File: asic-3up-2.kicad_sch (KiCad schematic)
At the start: 64 parts, among them J16 Conn_01x01, J17 Conn_01x01, J8 Conn_01x01, J9 Conn_01x01, U57 MCP1824T-1202E/OT, U58 MCP1824T-1202E/OT, U59 MCP1824T-1202E/OT, U60 MCP1824T-0802E, U61 MCP1824T-0802E, U62 MCP1824T-0802E, U63 BM1362AC_MODE1, U64 BM1362AC_MODE0, U65 BM1362AC_MODE1

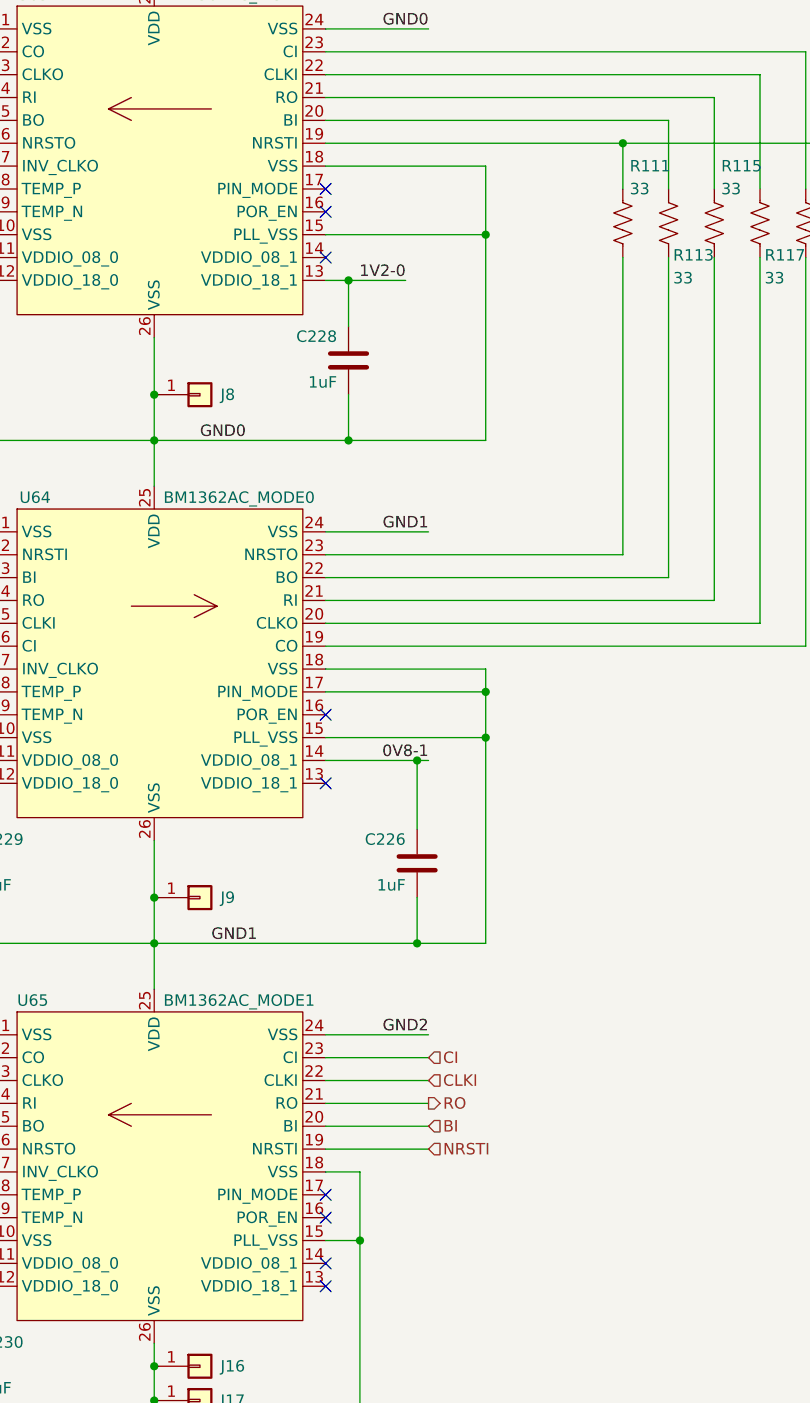
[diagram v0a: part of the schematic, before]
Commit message: fix PIN_MODE connections for #17
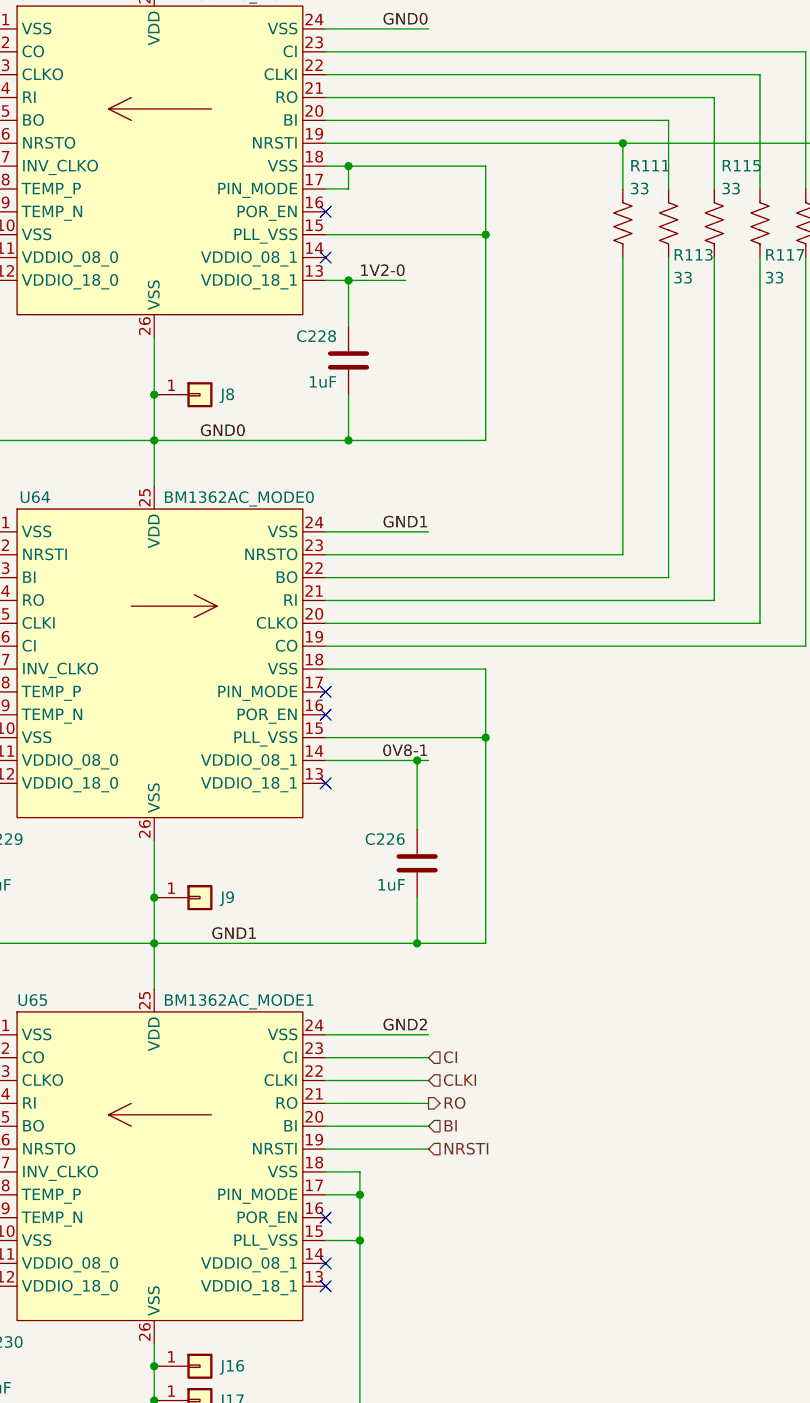
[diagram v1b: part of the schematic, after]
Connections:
- net GND0: now also U63.17 (PIN_MODE)
- net GND1: no longer U64.17 (PIN_MODE)
- net VSS: now also U65.17 (PIN_MODE)
- no-connect marks 26 -> 25
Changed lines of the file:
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@@
+	)
+	(junction
+		(at 271.78 186.69)
+		(diameter 0)
+		(color 0 0 0 0)
 	)
 	(junction
@@
 	)
 	(junction
-		(at 285.75 130.81)
-		(diameter 0)
-		(color 0 0 0 0)
-	)
-	(junction
 		(at 248.92 153.67)
 		(diameter 0)
@@
 	)
 	(junction
+		(at 270.51 72.39)
+		(diameter 0)
+		(color 0 0 0 0)
+	)
+	(junction
 		(at 87.63 137.16)
 		(diameter 0.9144)
@@
 	)
 	(no_connect
-		(at 267.97 186.69)
-	)
-	(no_connect
 		(at 267.97 82.55)
 	)
@@
 	)
 	(no_connect
+		(at 267.97 130.81)
+	)
+	(no_connect
 		(at 231.14 138.43)
 	)
@@
 	)
 	(no_connect
-		(at 267.97 74.93)
-	)
-	(no_connect
 		(at 66.04 185.42)
 	)
@@
 	(wire
 		(pts
-			(xy 285.75 72.39) (xy 267.97 72.39)
+			(xy 285.75 72.39) (xy 270.51 72.39)
+		)
+		(stroke
+			(width 0)
+			(type default)
+		)
+	)
+	(wire
+		(pts
+			(xy 270.51 72.39) (xy 267.97 72.39)
 		)
 		(stroke
@@
 	(wire
 		(pts
-			(xy 285.75 130.81) (xy 285.75 128.27)
+			(xy 267.97 186.69) (xy 271.78 186.69)
 		)
 		(stroke
@@
 	(wire
 		(pts
+			(xy 270.51 74.93) (xy 270.51 72.39)
+		)
+		(stroke
+			(width 0)
+			(type default)
+		)
+	)
+	(wire
+		(pts
 			(xy 219.71 82.55) (xy 220.98 82.55)
 		)
@@
 	(wire
 		(pts
+			(xy 267.97 74.93) (xy 270.51 74.93)
+		)
+		(stroke
+			(width 0)
+			(type default)
+		)
+	)
+	(wire
+		(pts
 			(xy 152.4 74.93) (xy 152.4 78.74)
 		)
@@
 	(wire
 		(pts
-			(xy 285.75 135.89) (xy 285.75 130.81)
+			(xy 285.75 128.27) (xy 285.75 135.89)
 		)
 		(stroke
@@
 	(wire
 		(pts
-			(xy 267.97 130.81) (xy 285.75 130.81)
-		)
-		(stroke
-			(width 0)
-			(type default)
-		)
-	)
-	(wire
-		(pts
 			(xy 270.51 85.09) (xy 267.97 85.09)
 		)
@@
 	(wire
 		(pts
+			(xy 271.78 186.69) (xy 271.78 191.77)
+		)
+		(stroke
+			(width 0)
+			(type default)
+		)
+	)
+	(wire
+		(pts
 			(xy 205.74 123.19) (xy 205.74 130.81)
 		)
@@
 	(wire
 		(pts
-			(xy 271.78 184.15) (xy 271.78 191.77)
-		)
-		(stroke
+			(xy 271.78 184.15) (xy 271.78 186.69)
+		)
+		(stroke

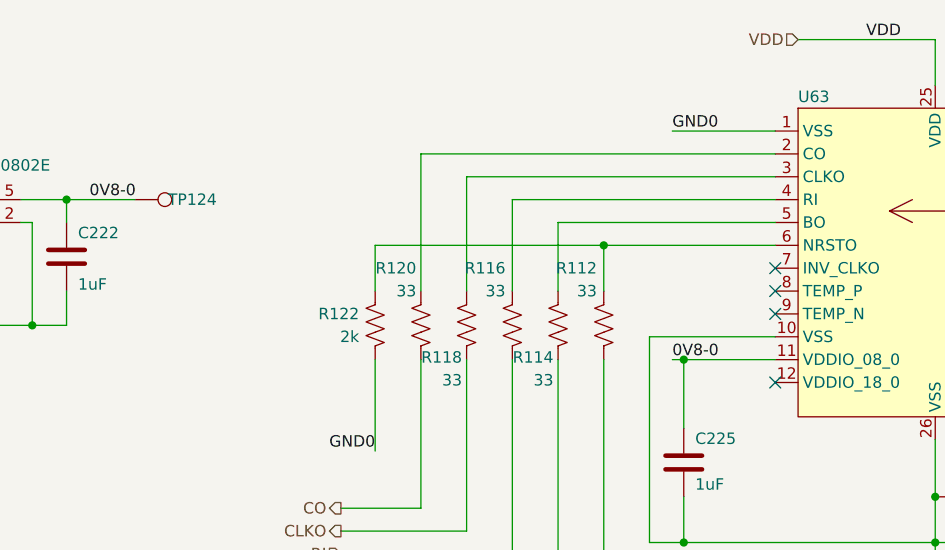
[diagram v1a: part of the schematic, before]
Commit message: added RI pullup resistors for #16. updated BOM. bumped version number to 3
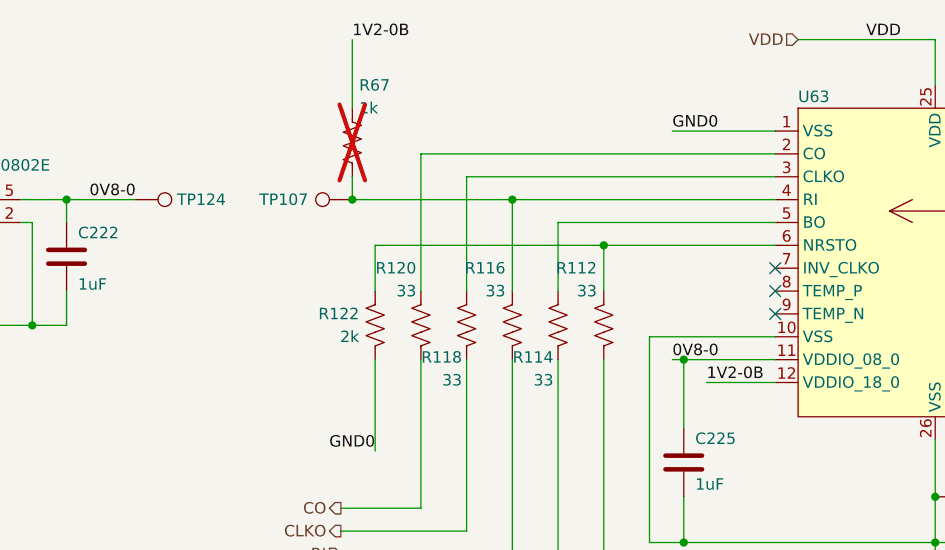
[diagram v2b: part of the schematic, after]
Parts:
- added R67: 1k, Resistor_SMD:R_0402_1005Metric, symbol Device:R_US
- added TP107: TestPoint, TestPoint:TestPoint_Pad_D1.0mm, symbol Connector:TestPoint
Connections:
- net 1V2-0B: now reaches U63.12 (VDDIO_18_0)
- net 1V2-0B: now also R67.1
- net at R116.1, U63.4 (RI): now also R67.2, TP107.1
- no-connect marks 25 -> 24
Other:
- title: (none) -> emberOne/00
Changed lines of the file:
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@@
 	(paper "A3")
 	(title_block
-		(date "2024-11-25")
-		(rev "2")
+		(title "emberOne/00")
+		(date "2025-02-25")
+		(rev "3")
 	)
 	(text "Reference Voltage Regulators"
@@
 	)
 	(junction
+		(at 201.93 64.77)
+		(diameter 0)
+		(color 0 0 0 0)
+	)
+	(junction
 		(at 356.87 114.3)
 		(diameter 0)
@@
 	)
 	(junction
+		(at 184.15 64.77)
+		(diameter 0)
+		(color 0 0 0 0)
+	)
+	(junction
 		(at 285.75 80.01)
 		(diameter 0)
@@
 	)
 	(no_connect
-		(at 231.14 85.09)
-	)
-	(no_connect
 		(at 231.14 184.15)
 	)
@@
 	(wire
 		(pts
+			(xy 184.15 46.99) (xy 184.15 54.61)
+		)
+		(stroke
+			(width 0)
+			(type default)
+		)
+	)
+	(wire
+		(pts
 			(xy 267.97 125.73) (xy 321.31 125.73)
 		)
@@
 	(wire
 		(pts
+			(xy 184.15 64.77) (xy 184.15 62.23)
+		)
+		(stroke
+			(width 0)
+			(type default)
+		)
+	)
+	(wire
+		(pts
 			(xy 270.51 85.09) (xy 267.97 85.09)
 		)
@@
 	(wire
 		(pts
+			(xy 184.15 64.77) (xy 201.93 64.77)
+		)
+		(stroke
+			(width 0)
+			(type default)
+		)
+	)
+	(wire
+		(pts
 			(xy 91.44 133.35) (xy 91.44 137.16)
 		)
@@
 	(wire
 		(pts
+			(xy 223.52 85.09) (xy 231.14 85.09)
+		)
+		(stroke
+			(width 0)
+			(type default)
+		)
+	)
+	(wire
+		(pts
 			(xy 248.92 153.67) (xy 248.92 158.75)
 		)
@@
 		)
 	)
+	(label "1V2-0B"
+		(at 184.15 46.99 0)
+		(effects
+			(font
+				(size 1.27 1.27)
+			)
+			(justify left bottom)
+		)
+	)
+	(label "1V2-0B"
+		(at 223.52 85.09 0)
+		(effects
+			(font
+				(size 1.27 1.27)
+			)
+			(justify left bottom)
+		)
+	)
 	(label "1V2-0"
 		(at 276.86 85.09 180)
@@
 	)
 	(symbol
+		(lib_id "Connector:TestPoint")
+		(at 184.15 64.77 90)
+		(mirror x)
+		(unit 1)
+		(exclude_from_sim no)
+		(in_bom no)
+		(on_board yes)
+		(dnp no)
+		(property "Reference" "TP107"
+			(at 176.53 64.77 90)
+			(effects
+				(font
+					(size 1.27 1.27)
+				)
+			)
+		)
+		(property "Value" "TestPoint"
+			(at 178.435 66.0399 90)
+			(effects
+				(font
+					(size 1.27 1.27)
+				)
+				(justify left)
+				(hide yes)
+			)
+		)
+		(property "Footprint" "TestPoint:TestPoint_Pad_D1.0mm"
+			(at 184.15 69.85 0)
+			(effects
+				(font
+					(size 1.27 1.27)
+				)
+				(hide yes)
+			)
+		)
+		(property "Datasheet" "~"
+			(at 184.15 69.85 0)
+			(effects
+				(font
+					(size 1.27 1.27)
+				)
+				(hide yes)
+			)
+		)
+		(property "Description" ""
+			(at 184.15 64.77 0)
+			(effects
+				(font
+					(size 1.27 1.27)
+				)
+				(hide yes)
+			)
+		)
+		(pin "1"
+		)
+		(instances
+			(project "emberone"
+				(path "/b036224c-4cdf-48cc-81df-19bc5283ebd2/b7ad7cc6-371f-46f9-875b-8b04bdc75b20"
+					(reference "TP107")
+					(unit 1)
+				)
+			)
+		)
+	)
+	(symbol
 		(lib_id "Device:C")
 		(at 346.71 72.39 0)
@@
 	)
 	(symbol
+		(lib_id "Device:R_US")
+		(at 184.15 58.42 0)
+		(unit 1)
+		(exclude_from_sim no)
+		(in_bom yes)
+		(on_board yes)
+		(dnp yes)
+		(property "Reference" "R67"
+			(at 184.912 52.07 0)
+			(effects
+				(font
+					(size 1.27 1.27)
+				)
+				(justify left)
+			)
+		)
+		(property "Value" "1k"
+			(at 184.912 54.61 0)
+			(effects
+				(font
+					(size 1.27 1.27)
+				)
+				(justify left)
+			)
+		)
+		(property "Footprint" "Resistor_SMD:R_0402_1005Metric"
+			(at 185.166 58.674 90)
+			(effects
+				(font
+					(size 1.27 1.27)
+				)
+				(hide yes)
+			)
+		)
+		(property "Datasheet" "~"
+			(at 184.15 58.42 0)
+			(effects
+				(font
+					(size 1.27 1.27)
+				)
+				(hide yes)
+			)
+		)
+		(property "Description" "Resistor, US symbol"
+			(at 184.15 58.42 0)
+			(effects
+				(font
+					(size 1.27 1.27)
+				)
+				(hide yes)
+			)
+		)
+		(property "DK" ""
+			(at 184.15 58.42 0)
+			(effects
+				(font
+					(size 1.27 1.27)
+				)
+				(hide yes)
+			)
+		)
+		(property "PARTNO" ""
+			(at 184.15 58.42 0)
+			(effects
+				(font
+					(size 1.27 1.27)
+				)
+				(hide yes)
+			)
+		)
+		(pin "1"
+		)
+		(pin "2"
+		)
+		(instances
+			(project "emberone"
+				(path "/b036224c-4cdf-48cc-81df-19bc5283ebd2/b7ad7cc6-371f-46f9-875b-8b04bdc75b20"
+					(reference "R67")
+					(unit 1)
+				)
+			)
+		)
+	)
+	(symbol
 		(lib_id "Device:C")
 		(at 220.98 93.98 0)
@@
 		(dnp no)
 		(property "Reference" "TP124"
-			(at 166.37 64.77 90)
+			(at 167.386 64.77 90)
 			(effects
 				(font

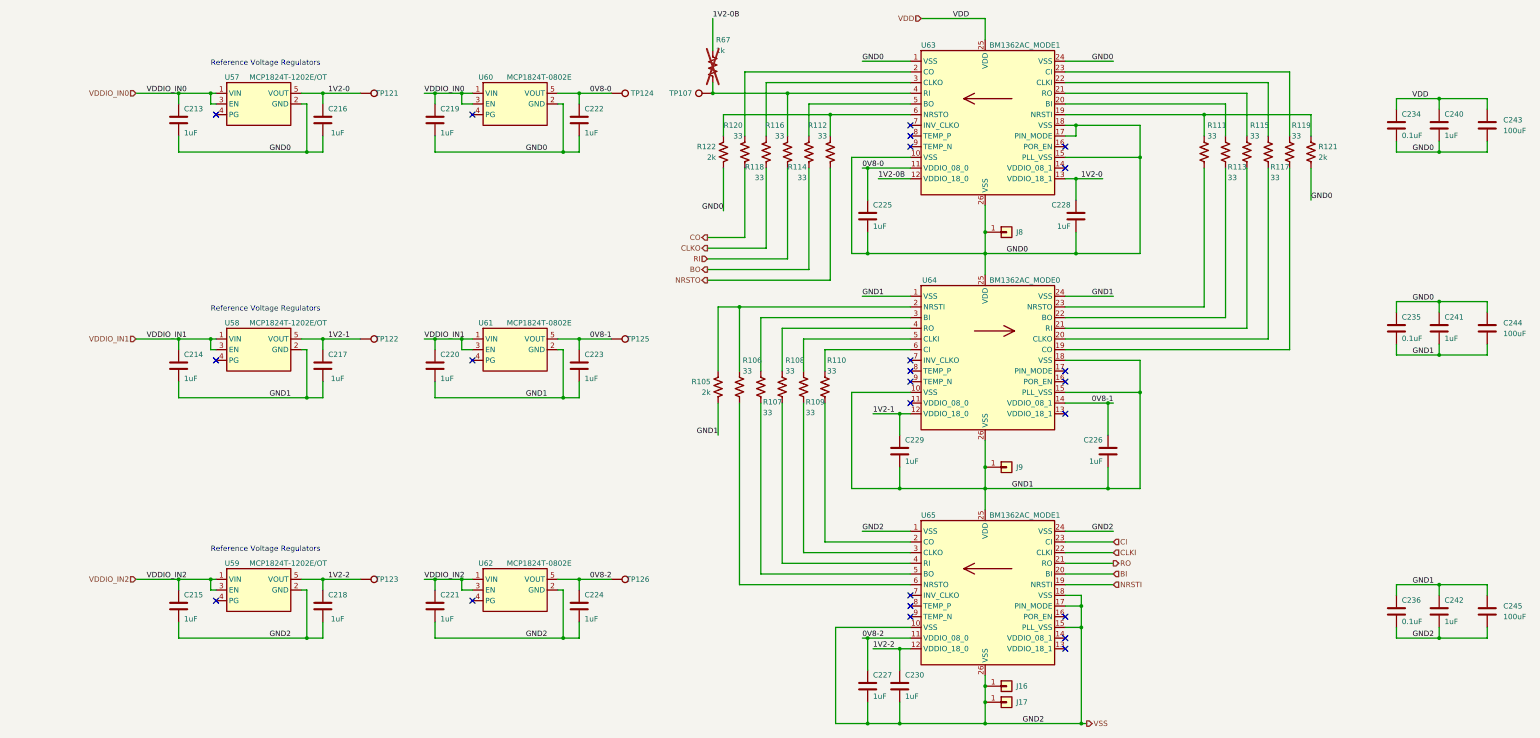
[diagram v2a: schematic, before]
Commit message: added fix for #22. deleted old gerbers
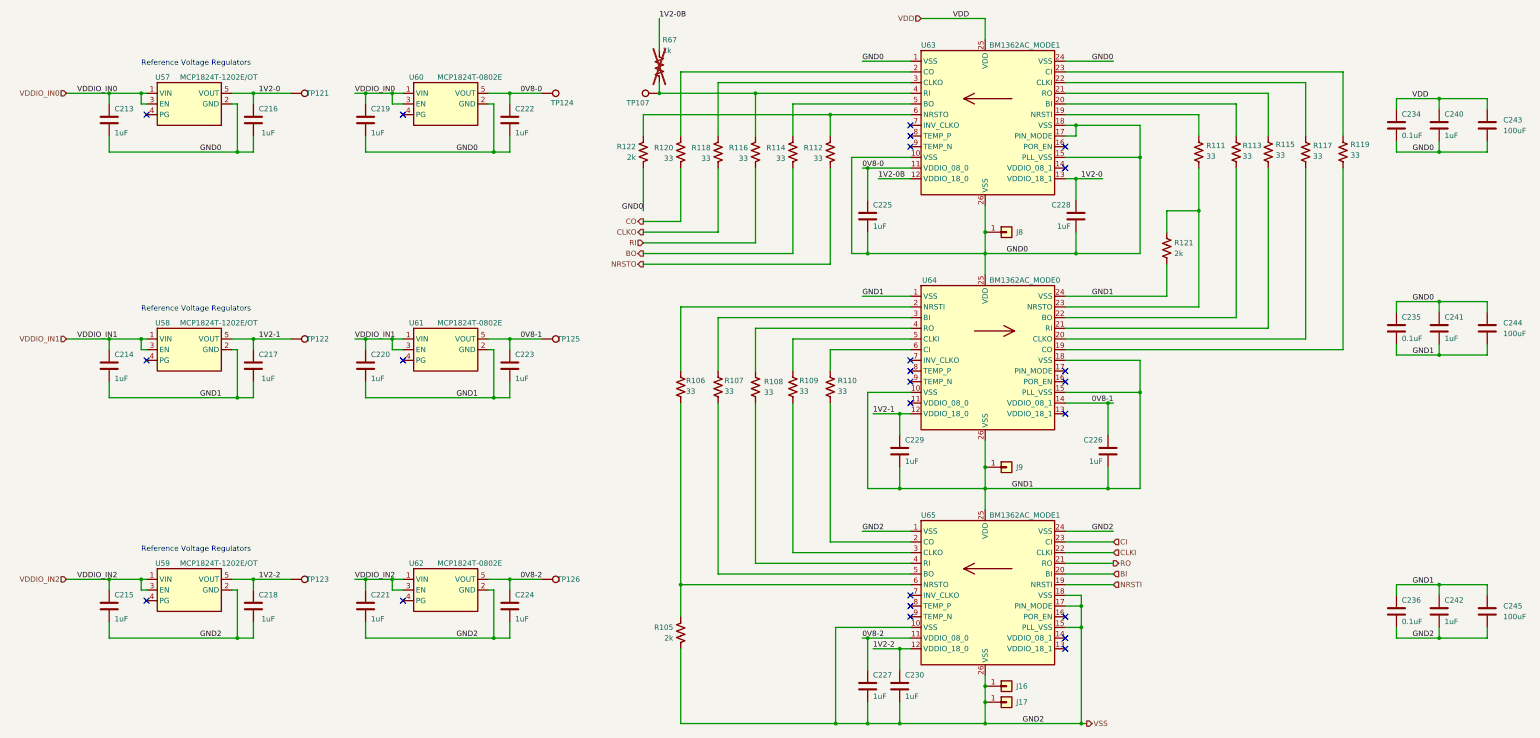
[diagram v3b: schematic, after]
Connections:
- net GND0: no longer R121.2
- net GND1: now also R121.2; no longer R105.2
- net VSS: now also R105.2
- net at R111.1, U63.19 (NRSTI): no longer R121.1
- net at R106.1, U64.2 (NRSTI): no longer R105.1
- net at R111.2, U64.23 (NRSTO): now also R121.1
- net at R106.2, U65.6 (NRSTO): now also R105.1
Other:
- moved on the sheet: C213, C214, C215, C216, C217, C218, C219, C220, C221, C222, C223, C224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

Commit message: DNP low side FET snubber circuit for now (to be redone in v4). Update current sense resistor filter values. regenerate BOM, iBOM. Slight slikscreen cleanup. regenerated gerbers
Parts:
- J16, J17, J8, J9: now left out of the parts list
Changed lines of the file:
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@@
 		(unit 1)
 		(exclude_from_sim no)
-		(in_bom yes)
+		(in_bom no)
 		(on_board yes)
 		(dnp no)
@@
 		(unit 1)
 		(exclude_from_sim no)
-		(in_bom yes)
+		(in_bom no)
 		(on_board yes)
 		(dnp no)
@@
 		(unit 1)
 		(exclude_from_sim no)
-		(in_bom yes)
+		(in_bom no)
 		(on_board yes)
 		(dnp no)
@@
 		(unit 1)
 		(exclude_from_sim no)
-		(in_bom yes)
-		(on_board yes)
-		(dnp no)
+		(in_bom no)
+		(on_board yes)
+		(dnp no)
